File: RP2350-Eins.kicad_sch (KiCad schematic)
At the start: 64 parts, among them J1 CONN_PWR, J10 CONN_USB, J2 CONN_ICSP, J3 CONN_A, J4 CONN_P, J5 CONN_X, J6 CONN_DBG, J7 CONN_JTAG, J8 CONN_D1, J9 CONN_D2, Q1 AO3401A, Q2 AO3400A, Q3 AO3400A, Q4 AO3400A, Q5 AO3400A, SW1 BOOTSEL, SW2 RESET, U1 W25Q128JVS, U2 RP2350A-QFN60, U3 AMS1117-5.0, U4 W25Q128JVEIQ, U5 AMS1117-3.3, Y1 12MHz

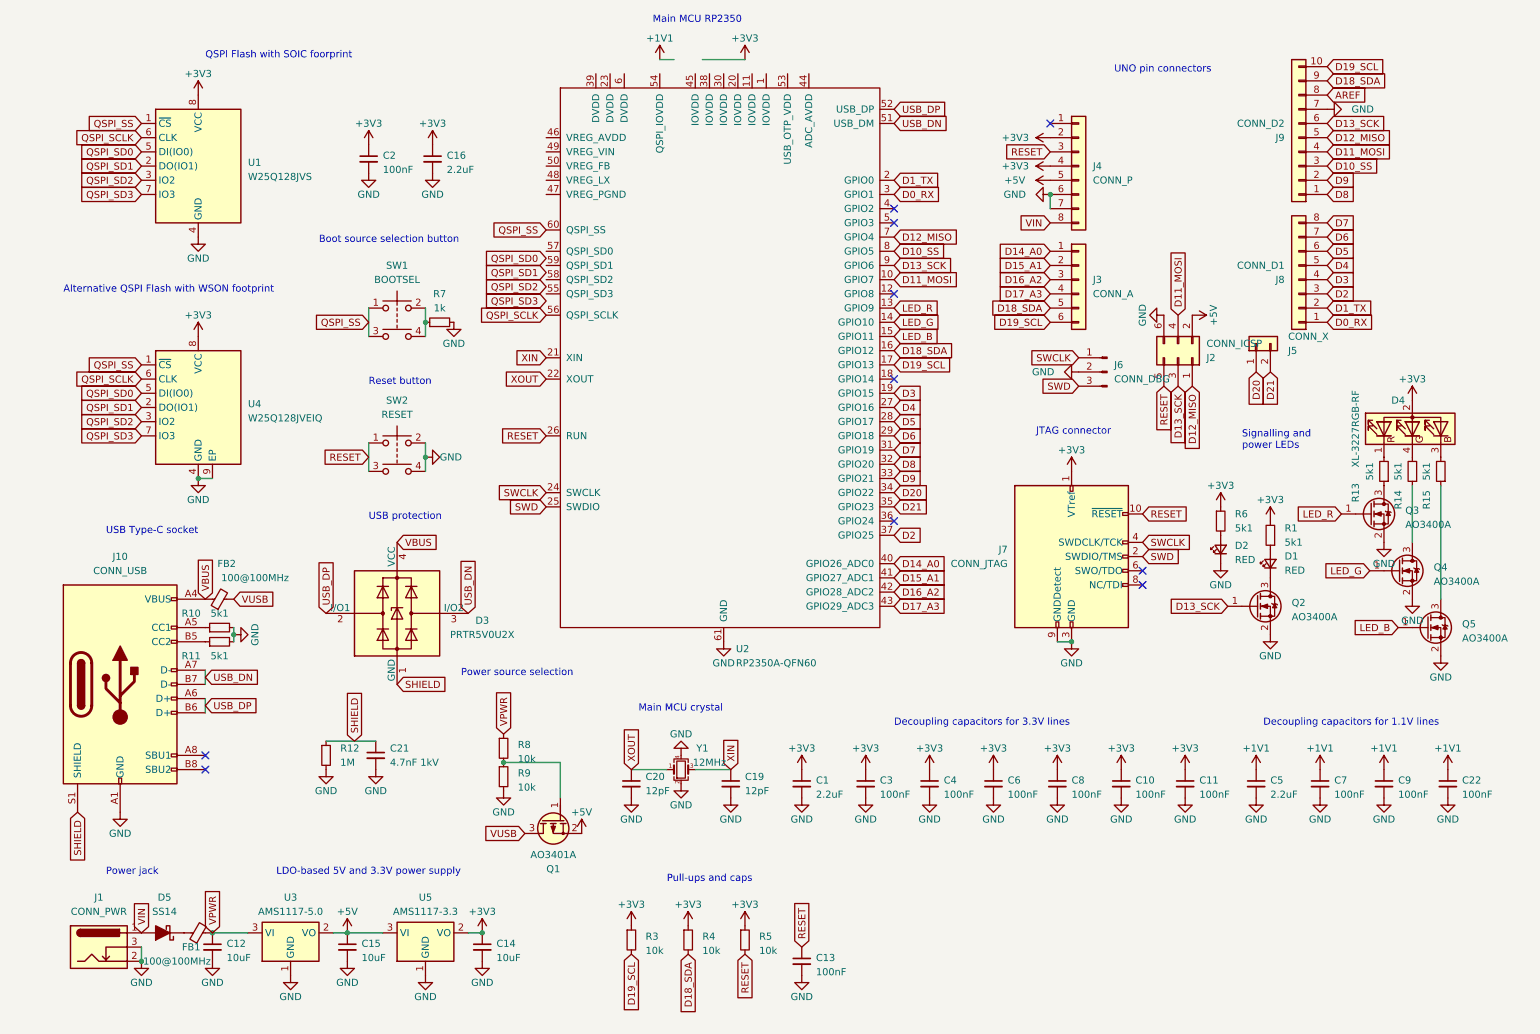
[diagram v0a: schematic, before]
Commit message: Added missing components. Routed the board.
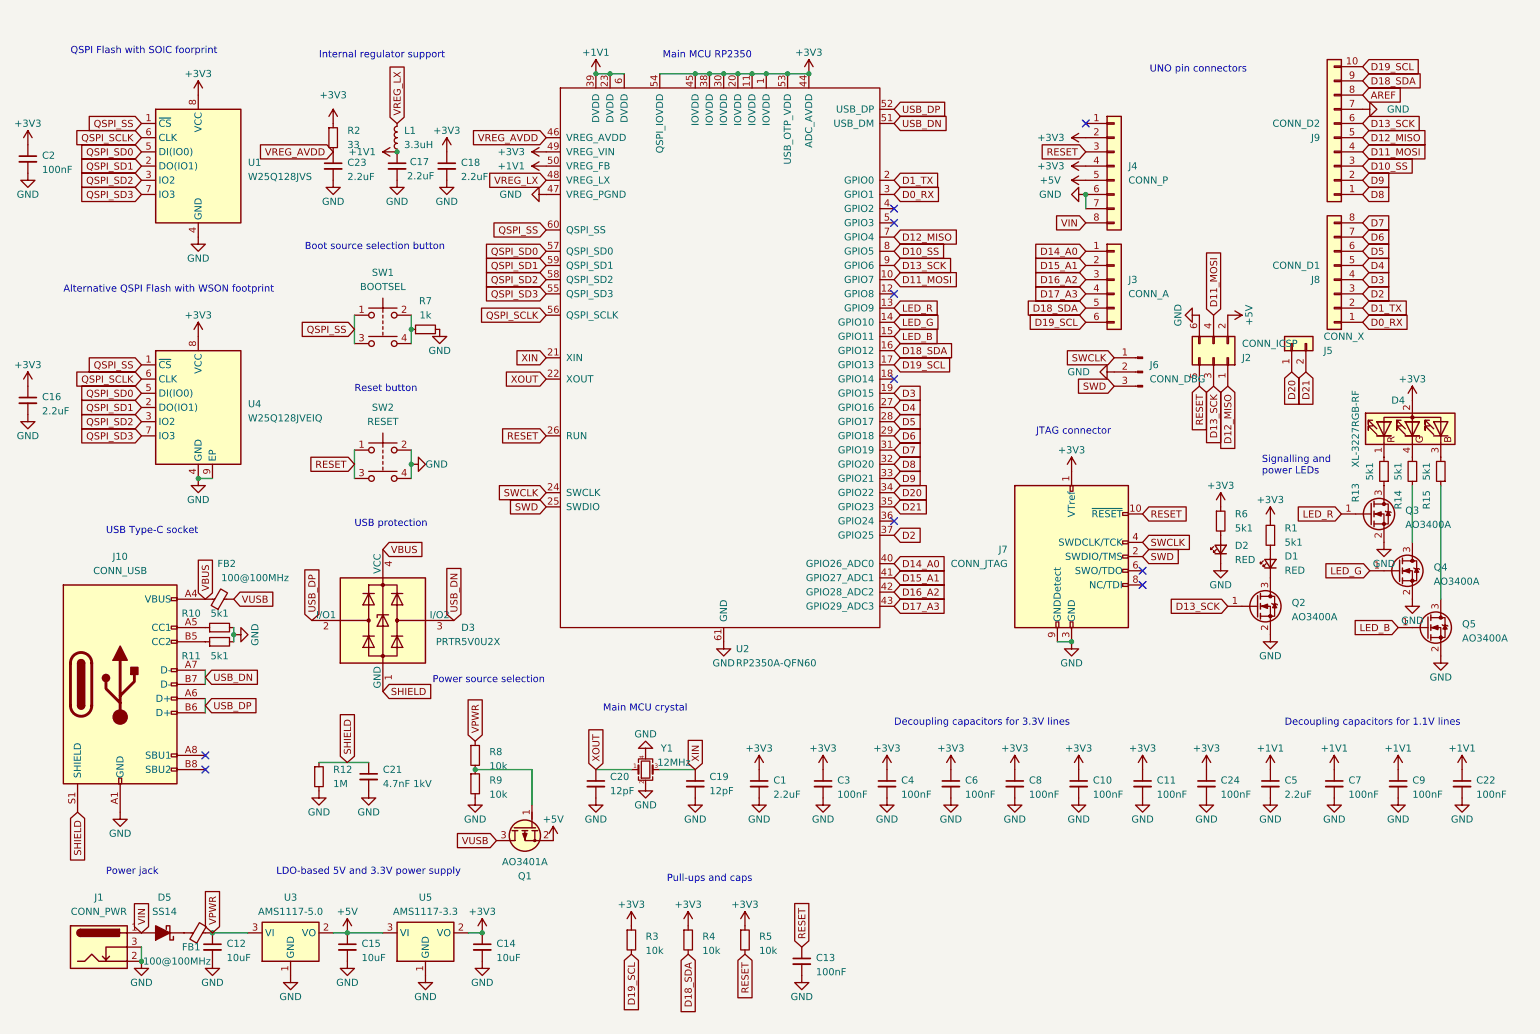
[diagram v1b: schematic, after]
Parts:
- added C17, C18, C23: 2.2uF, Capacitor_SMD:C_0603_1608Metric, symbol Device:C_Small
- added C24: 100nF, Capacitor_SMD:C_0402_1005Metric, symbol Device:C_Small
- added L1: 3.3uH, Inductor_SMD:L_0805_2012Metric, symbol Device:L_Small
- added R2: 33, Resistor_SMD:R_0402_1005Metric, symbol Device:R_Small
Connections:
- net +1V1: now also U2.23 (DVDD), U2.39 (DVDD), U2.50 (VREG_FB), U2.6 (DVDD), C17.1, L1.1
- net +3V3: now also U2.1 (IOVDD), U2.11 (IOVDD), U2.20 (IOVDD), U2.30 (IOVDD), U2.38 (IOVDD), U2.44 (ADC_AVDD), U2.45 (IOVDD), U2.49 (VREG_VIN), U2.53 (USB_OTP_VDD), U2.54 (QSPI_IOVDD), C18.1, C24.1, R2.1
- net GND: now also U2.47 (VREG_PGND), C17.2, C18.2, C23.2, C24.2
- net QSPI_SD0: now also U2.57 (QSPI_SD0)
- net QSPI_SD1: now also U2.59 (QSPI_SD1)
- net QSPI_SD2: now also U2.58 (QSPI_SD2)
- net QSPI_SD3: now also U2.55 (QSPI_SD3)
- net VREG_AVDD: now reaches U2.46 (VREG_AVDD)
- net VREG_AVDD: now also C23.1, R2.2
- net VREG_LX: now reaches U2.48 (VREG_LX)
- net VREG_LX: now also L1.2
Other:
- note added: "Internal regulator support"
- moved on the sheet: C1, C10, C11, C16, C19, C2, C20, C21, C22, C3, C4, C5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

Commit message: Moved staff around.
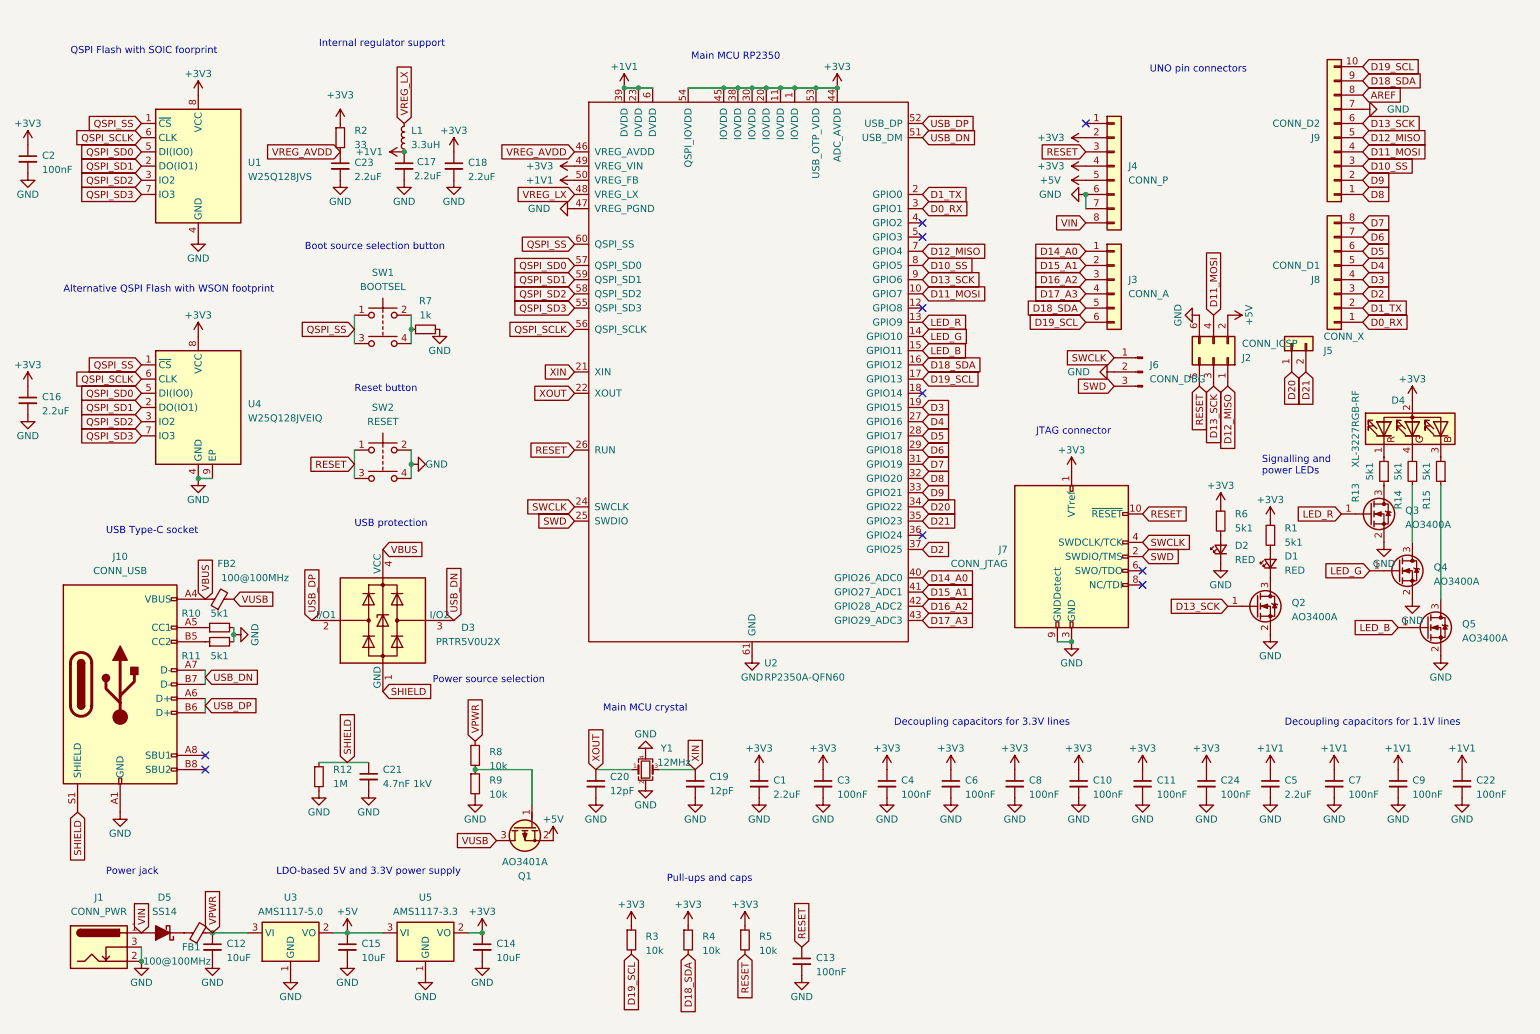
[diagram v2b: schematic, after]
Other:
- moved on the sheet: C17, C18, C23, L1, R2, U2
